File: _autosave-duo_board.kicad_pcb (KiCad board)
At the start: 2 copper layers, 167 x 122.9 mm, 49 parts, among them J1 PJ-342B-TX-SMT, U1 STM32F103RCTx

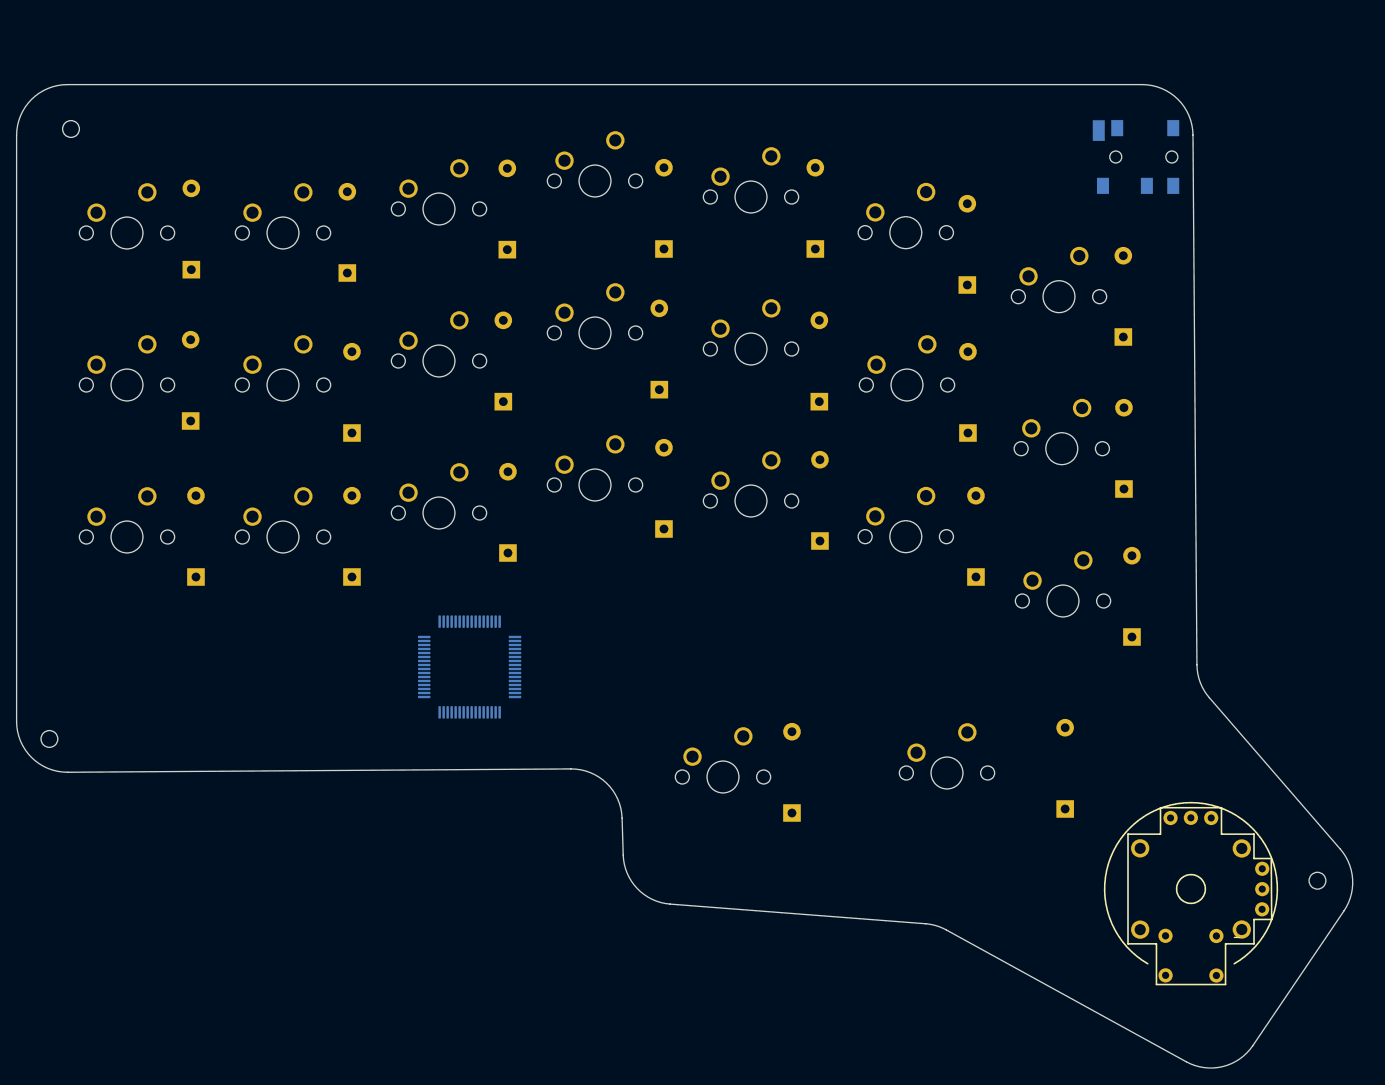
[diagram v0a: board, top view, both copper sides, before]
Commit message: completed MCU power supply
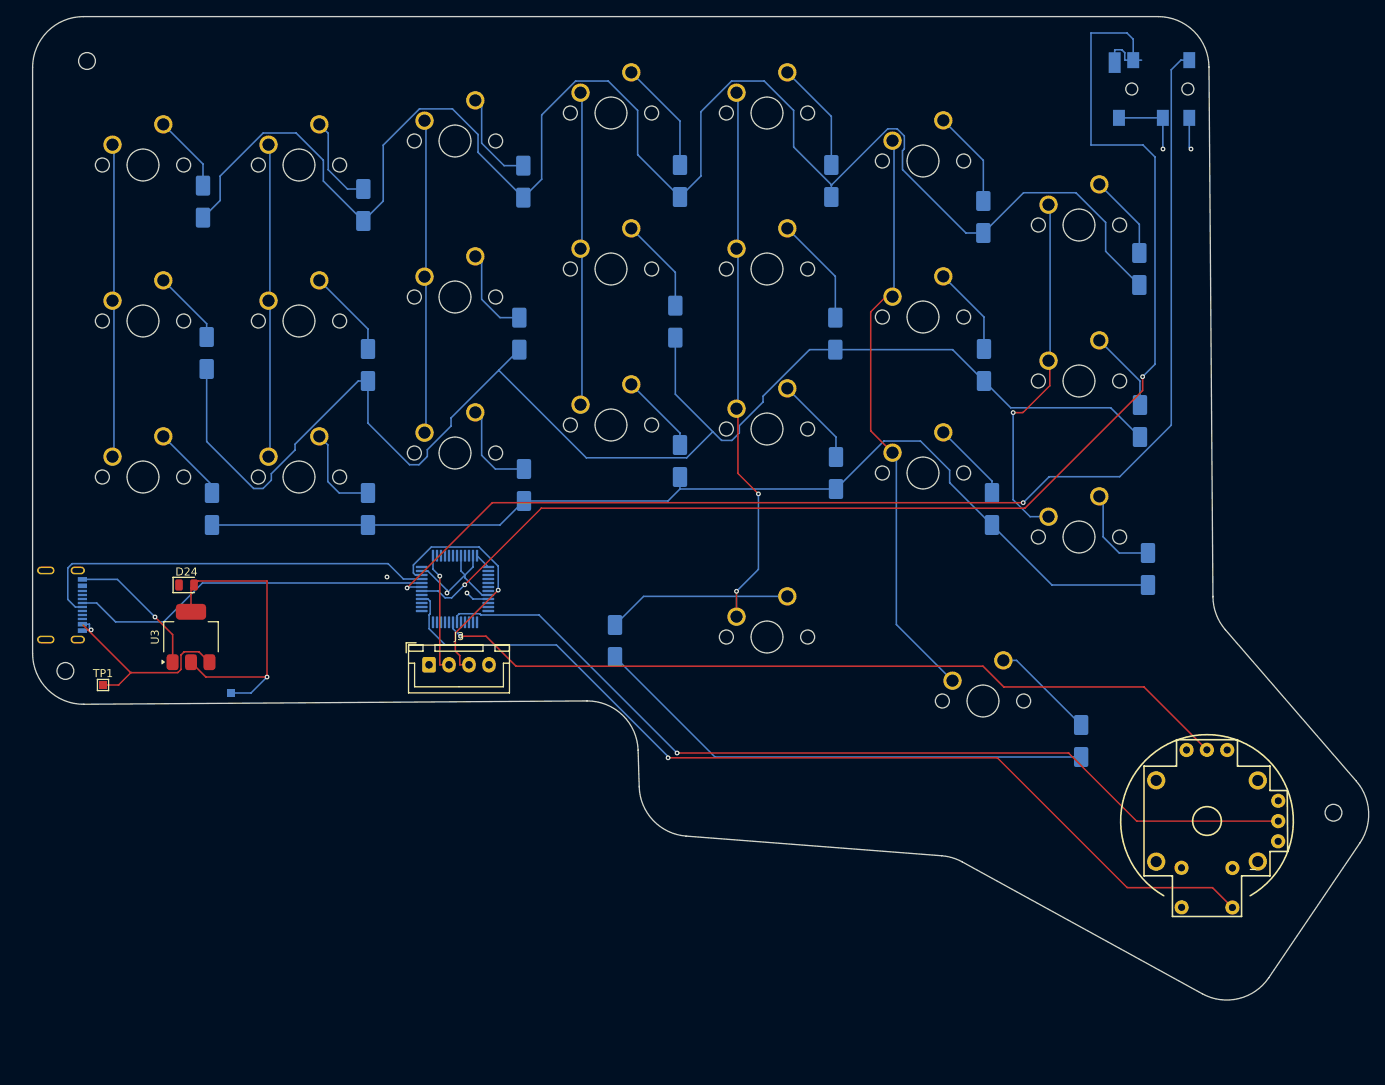
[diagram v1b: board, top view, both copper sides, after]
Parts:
- added D24: LED, LED_SMD:LED_0805_2012Metric, F.Cu at (81.4, 101.0)
- added J2: 2171790001, myCustomLibs:MOLEX_2171790001, B.Cu at (65.0, 103.5)
- added J3: Conn_01x04_Pin, Connector_JST:JST_XH_B4B-XH-A_1x04_P2.50mm_Vertical, F.Cu at (111.8, 111.0)
- added TP1: 5v TP, TestPoint:TestPoint_Pad_1.0x1.0mm, F.Cu at (71.0, 113.5)
- added TP2: 3V TP, TestPoint:TestPoint_Pad_1.0x1.0mm, B.Cu at (87.0, 114.5)
- added U3: AMS1117-3.3, Package_TO_SOT_SMD:SOT-223-3_TabPin2, F.Cu at (82.0, 107.5)
- D1, D10, D11, D12, D13, D14, D15, D16, D17, D18, D19, D2, D20, D21, D22, D23, D3, D4, D5, D6, D7, D8, D9: footprint Diode_THT:D_DO-41_SOD81_P10.16mm_Horizontal -> Diode_SMD:D_SMA
- J1: value PJ-342B-TX-SMT -> TRRS
- MX22: footprint PCM_marbastlib-mx:SW_MX_1.75u -> PCM_marbastlib-mx:SW_MX_1u
- MX23: footprint PCM_marbastlib-mx:SW_MX_1u -> PCM_marbastlib-mx:SW_MX_1.75u
- U1: value STM32F103RCTx -> STM32F103C8Tx; footprint Package_QFP:LQFP-64_10x10mm_P0.5mm -> Package_QFP:LQFP-48_7x7mm_P0.5mm
- moved MX12 86.7 mm to (154.0, 61.5)
- moved MX7 80.0 mm to (193.0, 56.0)
- moved MX11 60.7 mm to (134.5, 61.5)
- moved MX8 59.1 mm to (76.0, 68.0)
- moved MX10 57.6 mm to (115.0, 65.0)
- moved MX9 56.6 mm to (95.5, 68.0)
- moved MX4 53.3 mm to (134.5, 42.0)
- moved MX5 51.4 mm to (154.0, 42.0)
- moved MX3 51.1 mm to (115.0, 45.5)
- moved MX6 46.3 mm to (173.5, 48.0)
- moved MX20 45.5 mm to (173.5, 87.0)
- moved MX19 40.1 mm to (154.0, 81.5)
- moved D22 30.8 mm to (135.0, 108.0)
- moved MX14 28.5 mm to (193.0, 75.5)
- moved MX22 28.2 mm to (154.0, 107.5)
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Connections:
- J1 pad 2: unconnected-(J1-Pad2) -> USART1_RX
- J1 pad 3: unconnected-(J1-Pad3) -> USART1_TX
- J1 pad 4: unconnected-(J1-Pad4) -> USART1_TX
- J1 pad 5: unconnected-(J1-Pad5) -> GND
- J1 pad 6: unconnected-(J1-Pad6) -> +3.3V
- J1 pad 7: unconnected-(J1-Pad7) -> +3.3V
- MX10 pad 1: COL5 -> COL2
- MX10 pad 2: Net-(D13-A) -> Net-(D10-A)
- MX11 pad 1: COL6 -> COL3
- MX11 pad 2: Net-(D14-A) -> Net-(D11-A)
- MX12 pad 1: COL0 -> COL4
- MX12 pad 2: Net-(D15-A) -> Net-(D12-A)
- MX13 pad 1: COL4 -> COL5
- MX13 pad 2: Net-(D5-A) -> Net-(D13-A)
- MX14 pad 1: COL5 -> COL6
- MX14 pad 2: Net-(D6-A) -> Net-(D14-A)
- MX15 pad 1: COL1 -> COL0
- MX15 pad 2: Net-(D16-A) -> Net-(D15-A)
- MX16 pad 1: COL2 -> COL1
- MX16 pad 2: Net-(D17-A) -> Net-(D16-A)
- MX17 pad 1: COL3 -> COL2
- MX17 pad 2: Net-(D18-A) -> Net-(D17-A)
- MX18 pad 1: COL4 -> COL3
- MX18 pad 2: Net-(D19-A) -> Net-(D18-A)
- MX19 pad 1: COL6 -> COL4
- MX19 pad 2: Net-(D7-A) -> Net-(D19-A)
- MX20 pad 1: COL4 -> COL5
- MX20 pad 2: Net-(D22-A) -> Net-(D20-A)
- MX21 pad 1: COL5 -> COL6
- MX21 pad 2: Net-(D20-A) -> Net-(D21-A)
- MX22 pad 1: COL5 -> COL4
- MX22 pad 2: Net-(D23-A) -> Net-(D22-A)
- MX23 pad 1: COL6 -> COL5
- MX23 pad 2: Net-(D21-A) -> Net-(D23-A)
- MX3 pad 1: COL0 -> COL2
- MX3 pad 2: Net-(D8-A) -> Net-(D3-A)
- MX4 pad 1: COL1 -> COL3
- MX4 pad 2: Net-(D9-A) -> Net-(D4-A)
- MX5 pad 1: COL2 -> COL4
- MX5 pad 2: Net-(D10-A) -> Net-(D5-A)
- MX6 pad 1: COL3 -> COL5
- MX6 pad 2: Net-(D11-A) -> Net-(D6-A)
- MX7 pad 1: COL2 -> COL6
- MX7 pad 2: Net-(D3-A) -> Net-(D7-A)
- MX8 pad 1: COL3 -> COL0
- MX8 pad 2: Net-(D4-A) -> Net-(D8-A)
- MX9 pad 1: COL4 -> COL1
- MX9 pad 2: Net-(D12-A) -> Net-(D9-A)
- U1 pad 1: unconnected-(U1-VBAT-Pad1) -> +3.3V
- U1 pad 18: Net-(U1-VSS-Pad18) -> /X_AXIS
- U1 pad 19: unconnected-(U1-VDD-Pad19) -> /Y_AXIS
- U1 pad 23: unconnected-(U1-PA7-Pad23) -> GND
- U1 pad 24: unconnected-(U1-PC4-Pad24) -> +3.3V
- U1 pad 28: unconnected-(U1-PB2-Pad28) -> /BTN_PIN
- U1 pad 30: unconnected-(U1-PB11-Pad30) -> USART1_TX
- U1 pad 31: Net-(U1-VSS-Pad18) -> USART1_RX
- U1 pad 32: unconnected-(U1-VDD-Pad32) -> /USB_D-
- U1 pad 33: unconnected-(U1-PB12-Pad33) -> /USB_D+
- U1 pad 34: unconnected-(U1-PB13-Pad34) -> /SWDIO
- U1 pad 35: unconnected-(U1-PB14-Pad35) -> GND
- U1 pad 36: unconnected-(U1-PB15-Pad36) -> +3.3V
- U1 pad 37: unconnected-(U1-PC6-Pad37) -> /SWCLK
- U1 pad 44: unconnected-(U1-PA11-Pad44) -> GND
- U1 pad 47: Net-(U1-VSS-Pad18) -> GND
- U1 pad 48: unconnected-(U1-VDD-Pad48) -> +3.3V
- U1 pad 5: unconnected-(U1-PD0-Pad5) -> /HSE_IN
- U1 pad 6: unconnected-(U1-PD1-Pad6) -> /HSE_OUT
- U1 pad 7: unconnected-(U1-NRST-Pad7) -> /NRST
- U1 pad 8: unconnected-(U1-PC0-Pad8) -> GND
- U1 pad 9: unconnected-(U1-PC1-Pad9) -> +3.3V
- U2 pad B1A: unconnected-(U2-SEL+-PadB1A) -> /BTN_PIN
- U2 pad B2A: unconnected-(U2-SEL--PadB2A) -> GND
- U2 pad H1: unconnected-(U2-H+-PadH1) -> GND
- U2 pad H2: unconnected-(U2-H-PadH2) -> /Y_AXIS
- U2 pad H3: unconnected-(U2-H--PadH3) -> +3.3V
- U2 pad S1: Net-(U2-SHIELD-PadS1) -> GND
- U2 pad S2: Net-(U2-SHIELD-PadS1) -> GND
- U2 pad S3: Net-(U2-SHIELD-PadS1) -> GND
- U2 pad S4: Net-(U2-SHIELD-PadS1) -> GND
- U2 pad V1: unconnected-(U2-V+-PadV1) -> +3.3V
- U2 pad V2: unconnected-(U2-V-PadV2) -> /X_AXIS
- U2 pad V3: unconnected-(U2-V--PadV3) -> GND
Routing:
- net ROW0: track 0.00 -> 205.4 mm
- net ROW1: track 0.00 -> 181.9 mm
- net USART1_TX: track 0.00 -> 167.9 mm, vias 0 -> 2
- net USART1_RX: track 0.00 -> 153.0 mm, vias 0 -> 2
- net ROW2: track 0.00 -> 131.2 mm
- net /BTN_PIN: track 0.00 -> 119.6 mm, vias 0 -> 1
- net /X_AXIS: track 0.00 -> 114.3 mm, vias 0 -> 1
- net /Y_AXIS: track 0.00 -> 101.3 mm, vias 0 -> 1
- net COL5: track 0.00 -> 73.5 mm
- net COL4: track 0.00 -> 68.1 mm, vias 0 -> 2
- net ROW3: track 0.00 -> 63.4 mm
- net +3.3V: track 0.00 -> 54.8 mm, vias 0 -> 3
- net /USB_D+: track 0.00 -> 51.4 mm
- net /USB_D-: track 0.00 -> 45.4 mm
- net COL6: track 0.00 -> 45.0 mm, vias 0 -> 1
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- added copper zone on In2.Cu, net +3.3V
- added copper zone on In1.Cu, net GND
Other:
- copper layers 2 -> 4
